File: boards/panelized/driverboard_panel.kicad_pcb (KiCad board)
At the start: 2 copper layers, 49.5 x 54.6 mm, 44 parts, among them J1 RJ45, J2 RJ45, P1 HE10-10, Q1 NDS355, Q2 NDS355, Q3 NDS355, Q4 NDS355, Q5 NDS355, Q6 NDS355, Q7 NDS355, Q8 NDS355, U1 74HC595, U2 TS2937

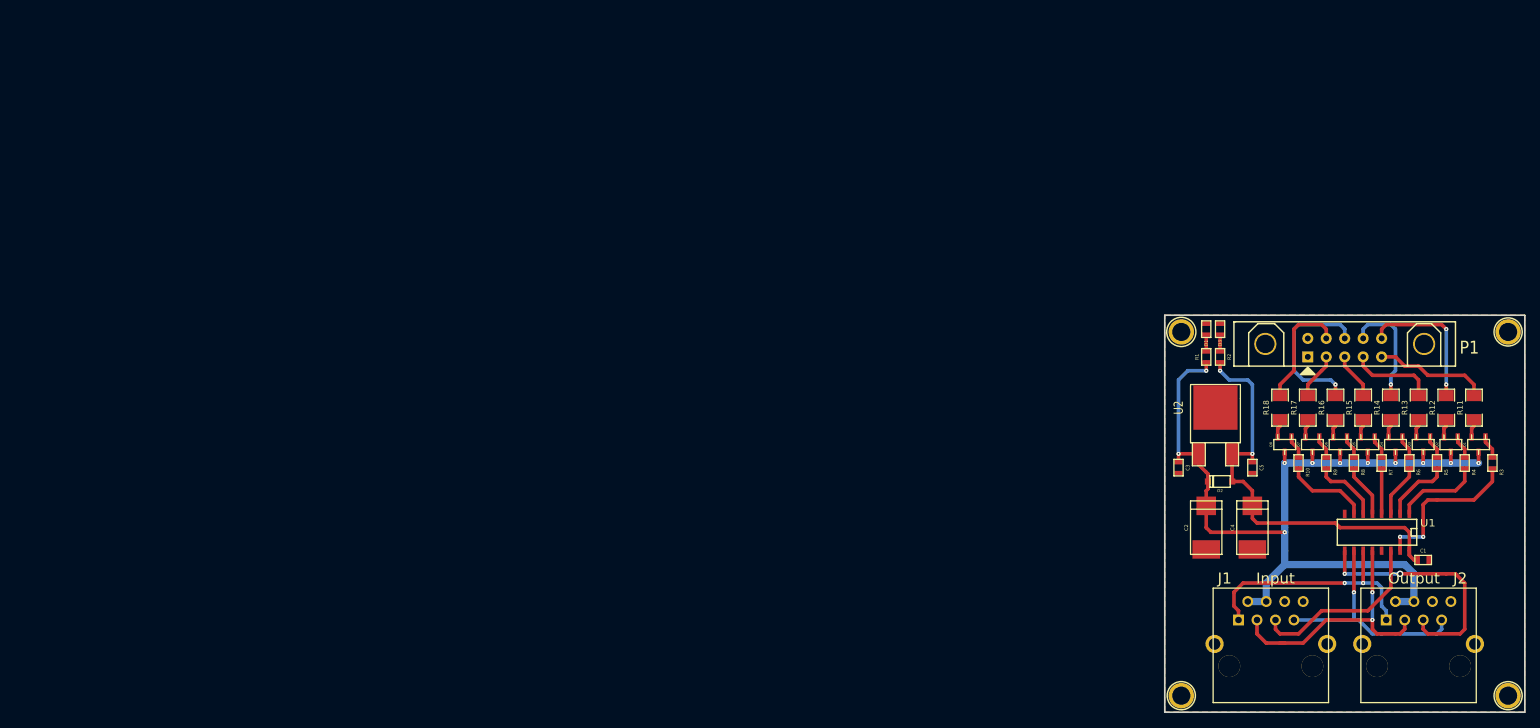
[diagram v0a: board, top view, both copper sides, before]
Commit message: Panelized boards
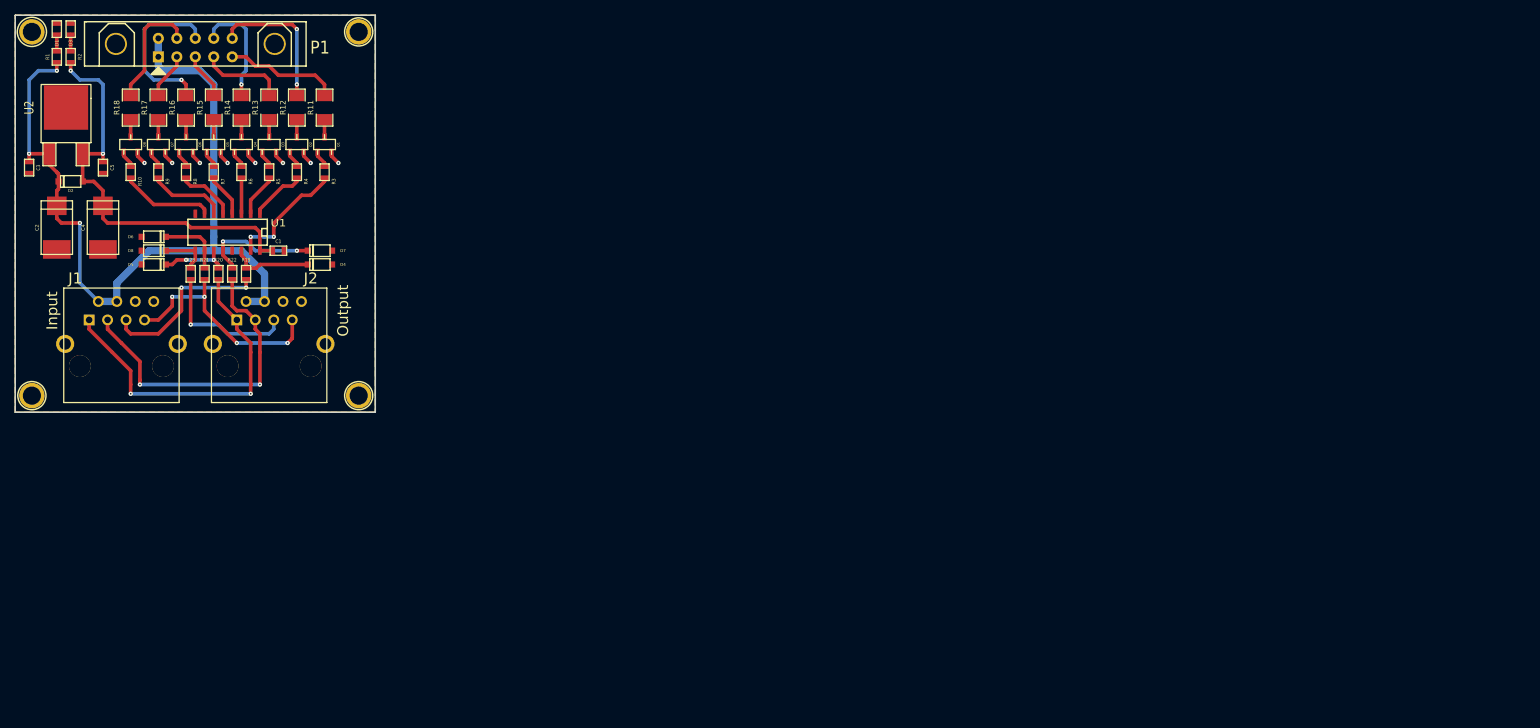
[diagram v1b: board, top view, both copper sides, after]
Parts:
- added D4: ZENER, sod123, F.Cu at (222.2, 49.5)
- added D5: ZENER, sod123, F.Cu at (199.4, 49.5)
- added D6: ZENER, sod123, F.Cu at (199.4, 45.7)
- added D7: ZENER, sod123, F.Cu at (222.2, 47.6)
- added D8: ZENER, sod123, F.Cu at (199.4, 47.6)
- added R19: 1k, SM0603, F.Cu at (212.1, 50.8)
- added R20: 1k, SM0603, F.Cu at (208.3, 50.8)
- added R21: 1k, SM0603, F.Cu at (206.4, 50.8)
- added R22: 1k, SM0603, F.Cu at (210.2, 50.8)
- added R23: 1k, SM0603, F.Cu at (204.5, 50.8)
- R10, R3, R4, R5, R6, R7, R8, R9: value 200 -> 220
- moved R3 165.6 mm to (222.9, 36.8)
- moved R4 165.6 mm to (219.1, 36.8)
- moved R5 165.6 mm to (215.3, 36.8)
- moved R10 165.6 mm to (196.2, 36.8)
- moved R6 165.6 mm to (211.5, 36.8)
- moved R7 165.6 mm to (207.6, 36.8)
- moved R8 165.6 mm to (203.8, 36.8)
- moved R9 165.6 mm to (200.0, 36.8)
- moved Q1 164.0 mm to (222.9, 33.0), turned to 0 degrees
- moved Q2 164.0 mm to (219.1, 33.0), turned to 0 degrees
- moved Q3 164.0 mm to (215.3, 33.0), turned to 0 degrees
- moved Q4 164.0 mm to (211.5, 33.0), turned to 0 degrees
- moved Q5 164.0 mm to (207.6, 33.0), turned to 0 degrees
- moved Q6 164.0 mm to (203.8, 33.0), turned to 0 degrees
- moved Q7 164.0 mm to (200.0, 33.0), turned to 0 degrees
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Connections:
- P1 pad 1: GND -> +24V
- P1 pad 2: GND -> +24V
- Q1 pad 2: +24V -> N-0000022
- Q1 pad 3: N-0000011 -> GND
- Q2 pad 2: +24V -> N-0000024
- Q2 pad 3: N-0000022 -> GND
- Q3 pad 2: +24V -> N-0000019
- Q3 pad 3: N-000003 -> GND
- Q4 pad 2: +24V -> N-0000017
- Q4 pad 3: N-000005 -> GND
- Q5 pad 2: +24V -> N-0000025
- Q5 pad 3: N-000007 -> GND
- Q6 pad 2: +24V -> N-0000027
- Q6 pad 3: N-0000010 -> GND
- Q7 pad 2: +24V -> N-0000036
- Q7 pad 3: N-0000034 -> GND
- Q8 pad 2: +24V -> N-0000034
- Q8 pad 3: N-0000037 (its old number) -> GND
- R11 pad 1: N-0000011 -> N-0000022
- R12 pad 1: N-0000022 -> N-0000024
- R13 pad 1: N-000003 -> N-0000019
- R14 pad 1: N-000005 -> N-0000017
- R15 pad 1: N-000007 -> N-0000025
- R16 pad 1: N-0000010 -> N-0000027
- R17 pad 1: N-0000034 -> N-0000036
- R18 pad 1: N-0000037 (its old number) -> N-0000034
- U1 pad 10: Reset -> N-0000029
- U1 pad 11: Clock -> N-0000030
- U1 pad 12: Enable -> N-0000033
- U1 pad 14: Data_In -> N-0000032
- U1 pad 9: Data_Out -> N-0000031
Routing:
- net N-0000033: track 0.00 -> 16.4 mm, vias 0 -> 2
- net GND: track 0.00 -> 15.0 mm, vias 0 -> 8
- net Data_Out: track 34.1 -> 19.7 mm, vias 2 -> 1
- net +24V: track 127.2 -> 114.6 mm, vias 11 -> 3
- net Clock: track 34.3 -> 46.6 mm
- net N-0000032: track 0.00 -> 11.4 mm
- net N-0000030: track 0.00 -> 9.52 mm, vias 0 -> 2
- net N-0000029: track 0.00 -> 9.26 mm
- net Enable: track 37.3 -> 44.0 mm
- net N-0000031: track 0.00 -> 6.72 mm
- net FET_1: track 22.1 -> 16.8 mm
- net FET_2: track 12.0 -> 7.80 mm
- net FET_3: track 9.44 -> 6.01 mm
- net N-000007: track 2.50 -> 0.00 mm
- net N-000005: track 2.50 -> 0.00 mm
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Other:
- board text added: "Version 1.1"
- board text removed: "Version 1.0"

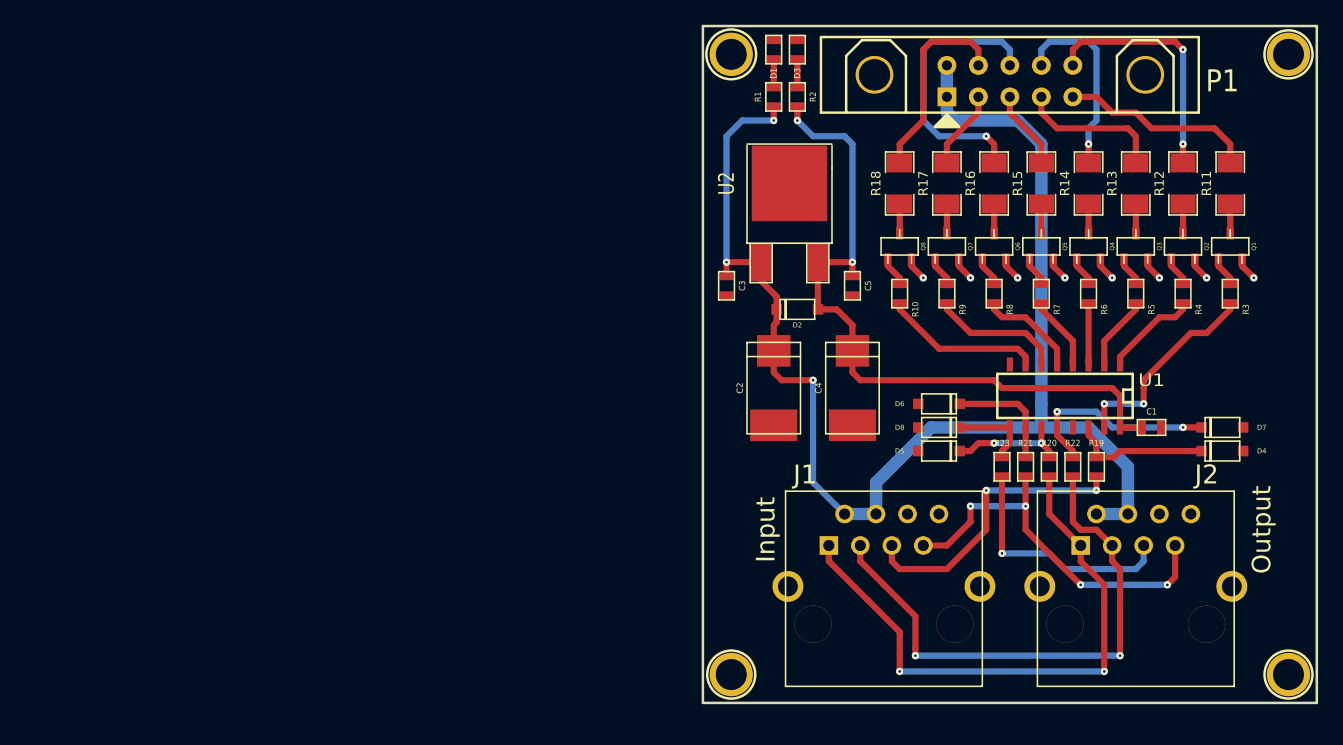
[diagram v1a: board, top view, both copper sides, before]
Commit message: Added logos
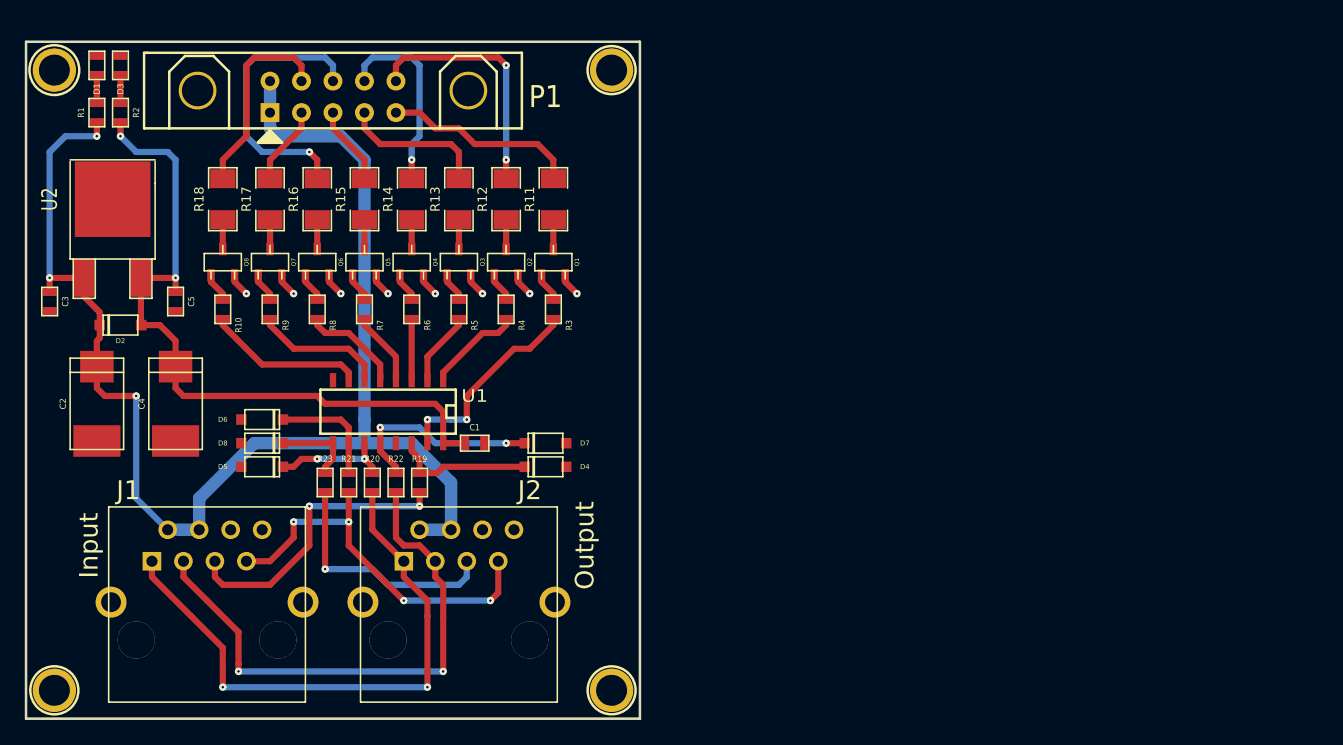
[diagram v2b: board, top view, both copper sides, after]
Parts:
- added G***: logo_hacker_silkbot_10_00mm, logo_hacker_silkbot_10_00mm, B.Cu at (139.7, 48.9)
- moved 1PIN 54.6 mm to (128.0, 18.8)
- moved 1PIN 54.6 mm to (128.0, 68.8)
- moved 1PIN 54.6 mm to (173.0, 68.8)
- moved 1PIN 54.6 mm to (173.0, 18.8)
- moved C2 54.6 mm to (131.4, 45.7)
- moved C4 54.6 mm to (137.8, 45.7)
- moved C5 54.6 mm to (137.8, 37.5)
- moved D1 54.6 mm to (131.4, 18.4)
- moved D2 54.6 mm to (133.3, 39.4)
- moved D3 54.6 mm to (133.3, 18.4)
- moved D4 54.6 mm to (167.6, 50.8)
- moved D7 54.6 mm to (167.6, 48.9)
- moved Q4 54.6 mm to (156.8, 34.3)
- moved Q5 54.6 mm to (153.0, 34.3)
- moved Q6 54.6 mm to (149.2, 34.3)
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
